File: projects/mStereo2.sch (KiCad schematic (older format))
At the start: 27 parts, among them P101 CONN_AMANERO, P102 MOLEX KK 1x2, P103 MOLEX KK 1X3, P104 NC3MAHL, P105 NC3MAHL, U101 ISO7640, U102 CDCLVC1104, U103 MCP100-315DI, U104 SRC4192, X101 XTAL

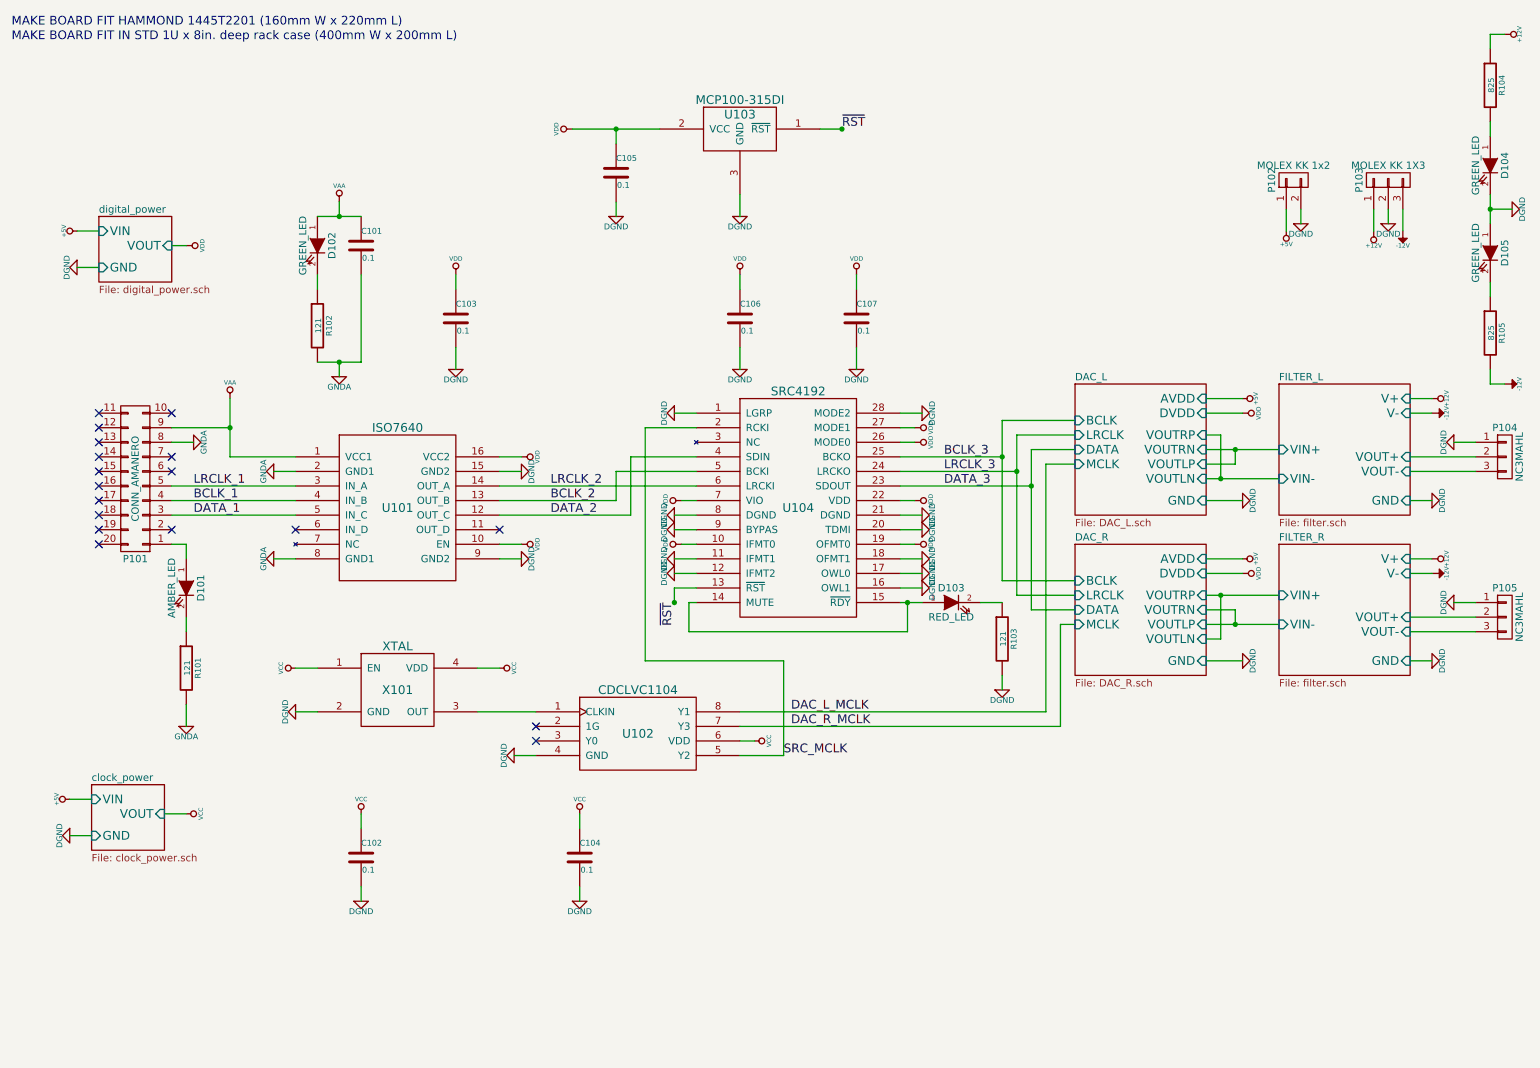
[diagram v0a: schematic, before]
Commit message: update XLR connector part.  Netlist now outdated.
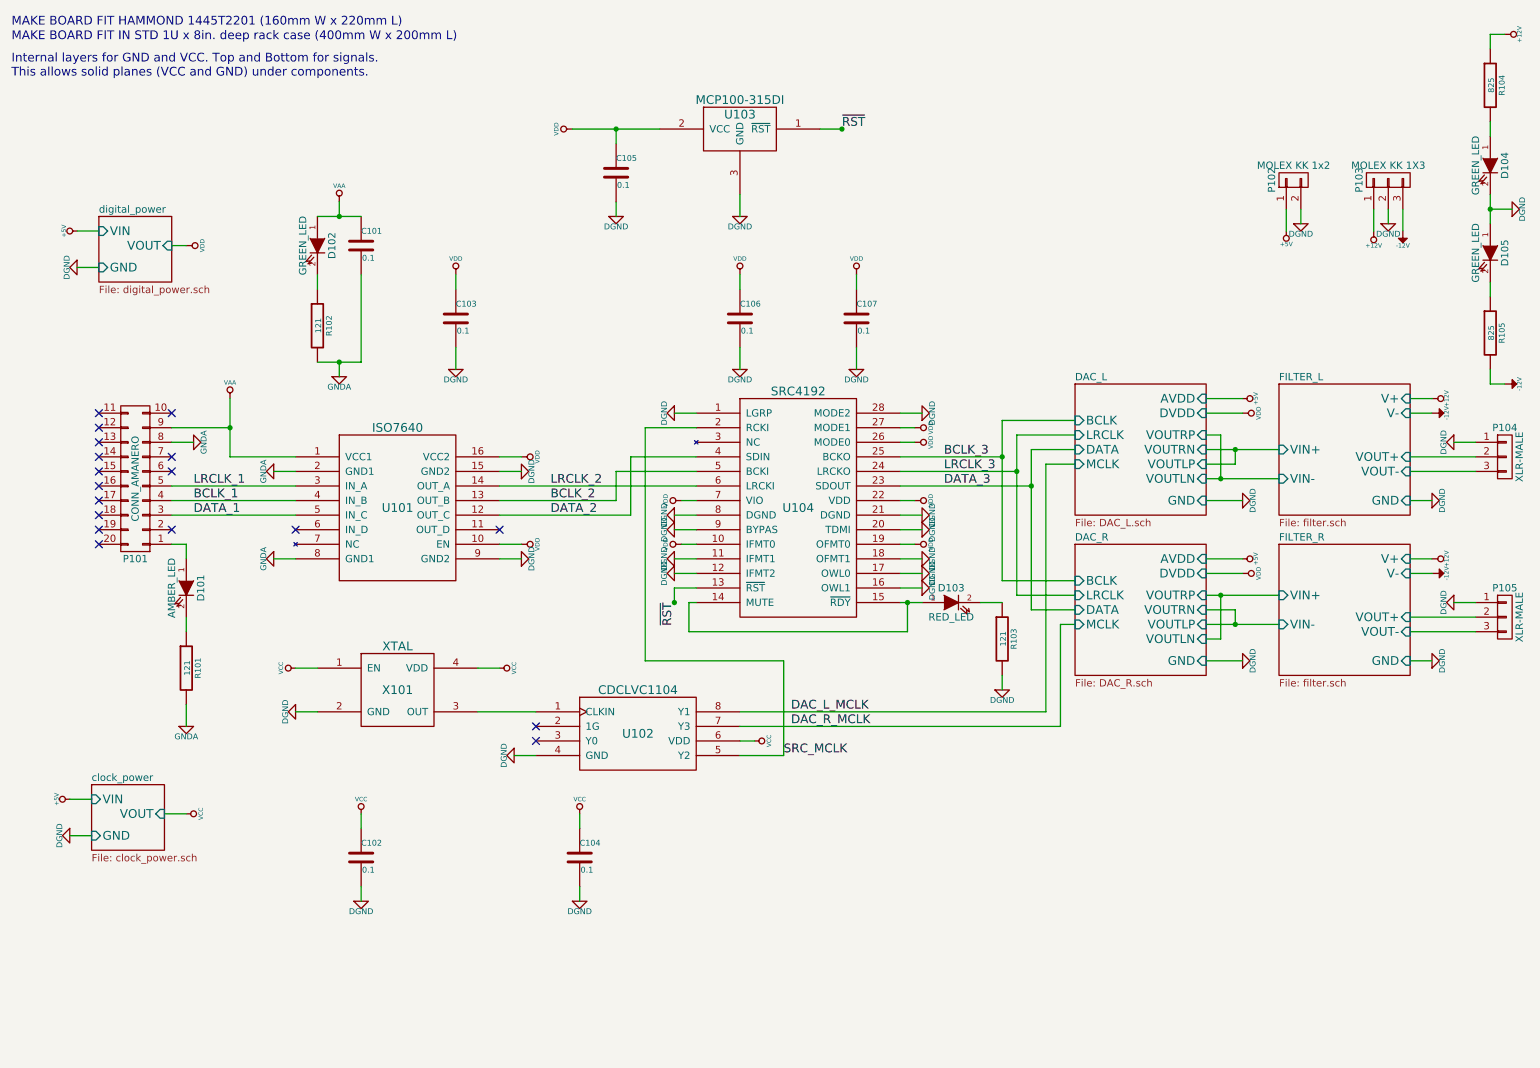
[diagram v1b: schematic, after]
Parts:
- P104, P105: value NC3MAHL -> XLR-MALE; Description XLR connectors 3C MALE COMBO -> XLR Connectors 3P MALE CHASS HORIZONTAL 1; Manu-PN NC3MAHL -> NC3MAAH-1; Supplier-PN 568-NC3MAHL -> 568-NC3MAAH-1
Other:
- note added: "Internal layers for GND and VCC. Top and Bottom for signals.\nThis allows solid planes (VCC and GND) under components."
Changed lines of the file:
@@
 LIBS:oscillator_gosselin
 LIBS:wolfson_gosselin
-LIBS:analog_devices_gosselin
 LIBS:power
 LIBS:device
@@
 LIBS:microchip_gosselin
 LIBS:linear_technology_gosselin
+LIBS:led_gosselin
 LIBS:mStereo2-cache
 EELAYER 24 0
@@
 P 10800 3600
 F 0 "P104" H 10800 3800 50  0000 C CNN
-F 1 "NC3MAHL" V 10900 3600 50  0000 C CNN
+F 1 "XLR-MALE" V 10900 3600 50  0000 C CNN
 F 2 "" H 10800 3600 60  0000 C CNN
 F 3 "" H 10800 3600 60  0000 C CNN
 F 4 "Mouser" H 10800 3600 60  0001 C CNN "Supplier"
-F 5 "568-NC3MAHL" H 10800 3600 60  0001 C CNN "Supplier-PN"
+F 5 "568-NC3MAAH-1" H 10800 3600 60  0001 C CNN "Supplier-PN"
 F 6 "Neutrik" H 10800 3600 60  0001 C CNN "Manu"
-F 7 "NC3MAHL" H 10800 3600 60  0001 C CNN "Manu-PN"
-F 8 "XLR connectors 3C MALE COMBO" H 10800 3600 60  0001 C CNN "Description"
+F 7 "NC3MAAH-1" H 10800 3600 60  0001 C CNN "Manu-PN"
+F 8 "XLR Connectors 3P MALE CHASS HORIZONTAL 1" H 10800 3600 60  0001 C CNN "Description"
 	1    10800 3600
 	1    0    0    -1
@@
 	1    0    0    -1
 $EndComp
-$Comp
-L CONN_01X03 P105
-U 1 1 543297CE
-P 10800 4700
-F 0 "P105" H 10800 4900 50  0000 C CNN
-F 1 "NC3MAHL" V 10900 4700 50  0000 C CNN
-F 2 "" H 10800 4700 60  0000 C CNN
-F 3 "" H 10800 4700 60  0000 C CNN
-F 4 "Mouser" H 10800 4700 60  0001 C CNN "Supplier"
-F 5 "568-NC3MAHL" H 10800 4700 60  0001 C CNN "Supplier-PN"
-F 6 "Neutrik" H 10800 4700 60  0001 C CNN "Manu"
-F 7 "NC3MAHL" H 10800 4700 60  0001 C CNN "Manu-PN"
-F 8 "XLR connectors 3C MALE COMBO" H 10800 4700 60  0001 C CNN "Description"
-	1    10800 4700
-	1    0    0    -1
-$EndComp
 Text Notes 550  650  0    60   ~ 0
 MAKE BOARD FIT HAMMOND 1445T2201 (160mm W x 220mm L)
@@
 	2800 2950 2800 3050
 Wire Wire Line
-	2650 2950 2950 2950
+	2650 2950 2800 2950
+Wire Wire Line
+	2800 2950 2950 2950
 Connection ~ 2800 1950
 Wire Wire Line
 	2800 1850 2800 1950
 Wire Wire Line
-	2650 1950 2950 1950
+	2650 1950 2800 1950
+Wire Wire Line
+	2800 1950 2950 1950
 Wire Wire Line
 	2650 2350 2650 2450
@@
 	10700 3000 10700 3100
 Wire Wire Line
-	10700 1800 10700 2000
+	10700 1800 10700 1900
+Wire Wire Line
+	10700 1900 10700 2000
 Wire Wire Line
 	9900 1900 9900 2050
@@
 	4700 1450 4700 1350
 Wire Wire Line
-	4400 1350 5000 1350
+	4400 1350 4700 1350
+Wire Wire Line
+	4700 1350 5000 1350
 Wire Wire Line
 	10150 5000 10300 5000
@@
 Connection ~ 8950 3550
 Wire Wire Line
-	8750 4550 9250 4550
+	8750 4550 8850 4550
+Wire Wire Line
+	8850 4550 9250 4550
 Wire Wire Line
 	4450 6550 4450 6650
@@
 	2500 3900 1650 3900
 Wire Wire Line
-	2050 3200 2050 3600
+	2050 3200 2050 3400
+Wire Wire Line
+	2050 3400 2050 3600
 Wire Wire Line
 	1650 3800 2500 3800
@@
 	6700 4800 6700 4600
 Wire Wire Line
-	6650 4600 6800 4600
+	6650 4600 6700 4600
+Wire Wire Line
+	6700 4600 6800 4600
 Wire Wire Line
 	5100 3300 5250 3300
@@
 	6650 3600 7350 3600
 Wire Wire Line
-	7350 3350 7350 4450
+	7350 3350 7350 3600
+Wire Wire Line
+	7350 3600 7350 4450
 Wire Wire Line
 	7350 3350 7850 3350
@@
 	6650 3700 7450 3700
 Wire Wire Line
-	7450 3450 7450 4550
+	7450 3450 7450 3700
+Wire Wire Line
+	7450 3700 7450 4550
 Wire Wire Line
 	7450 3450 7850 3450
@@
 	6650 3800 7550 3800
 Wire Wire Line
-	7550 3550 7550 4650
+	7550 3550 7550 3800
+Wire Wire Line
+	7550 3800 7550 4650
 Wire Wire Line
 	7550 3550 7850 3550
@@
 	8850 3450 8850 3750
 Wire Wire Line
-	8750 3750 9250 3750
-Wire Wire Line
-	8750 3550 9250 3550
+	8750 3750 8850 3750
+Wire Wire Line
+	8850 3750 9250 3750
+Wire Wire Line
+	8750 3550 8950 3550
+Wire Wire Line
+	8950 3550 9250 3550
 Wire Wire Line
 	8950 3650 8950 3550
@@
 	8950 4750 8950 4650
 Wire Wire Line
-	8750 4750 9250 4750
+	8750 4750 8950 4750
+Wire Wire Line
+	8950 4750 9250 4750
 $Comp
 L DGND #PWR075
@@
 Text Notes 550  750  0    60   ~ 0
 MAKE BOARD FIT IN STD 1U x 8in. deep rack case (400mm W x 200mm L)
+Text Notes 550  1000 0    60   ~ 0
+Internal layers for GND and VCC. Top and Bottom for signals.\nThis allows solid planes (VCC and GND) under components.
+$Comp
+L CONN_01X03 P105
+U 1 1 54769445
+P 10800 4700
+F 0 "P105" H 10800 4900 50  0000 C CNN
+F 1 "XLR-MALE" V 10900 4700 50  0000 C CNN
+F 2 "" H 10800 4700 60  0000 C CNN
+F 3 "" H 10800 4700 60  0000 C CNN
+F 4 "Mouser" H 10800 4700 60  0001 C CNN "Supplier"
+F 5 "568-NC3MAAH-1" H 10800 4700 60  0001 C CNN "Supplier-PN"
+F 6 "Neutrik" H 10800 4700 60  0001 C CNN "Manu"
+F 7 "NC3MAAH-1" H 10800 4700 60  0001 C CNN "Manu-PN"
+F 8 "XLR Connectors 3P MALE CHASS HORIZONTAL 1" H 10800 4700 60  0001 C CNN "Description"
+	1    10800 4700
+	1    0    0    -1
+$EndComp
 $EndSCHEMATC

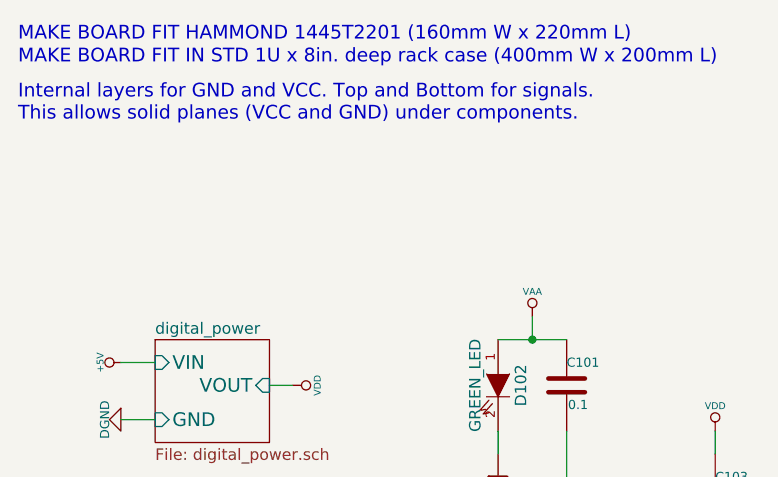
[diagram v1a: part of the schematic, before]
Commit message: update schematic notes
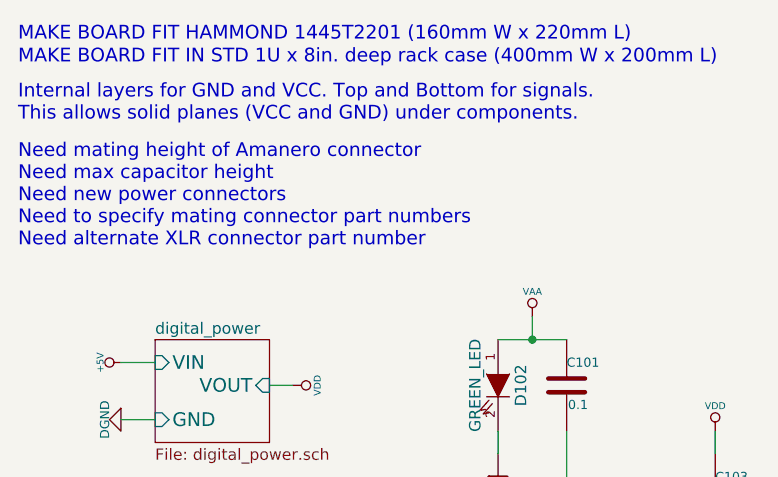
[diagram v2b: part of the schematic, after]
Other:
- note added: "Need mating height of Amanero connector\nNeed max capacitor height\nNeed new power connectors\nNeed to specify mating connector part numbers\nNeed alternate XLR connector part number\n"
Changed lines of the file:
@@
 	1    0    0    -1
 $EndComp
+Text Notes 550  1550 0    60   ~ 0
+Need mating height of Amanero connector\nNeed max capacitor height\nNeed new power connectors\nNeed to specify mating connector part numbers\nNeed alternate XLR connector part number\n
 $EndSCHEMATC

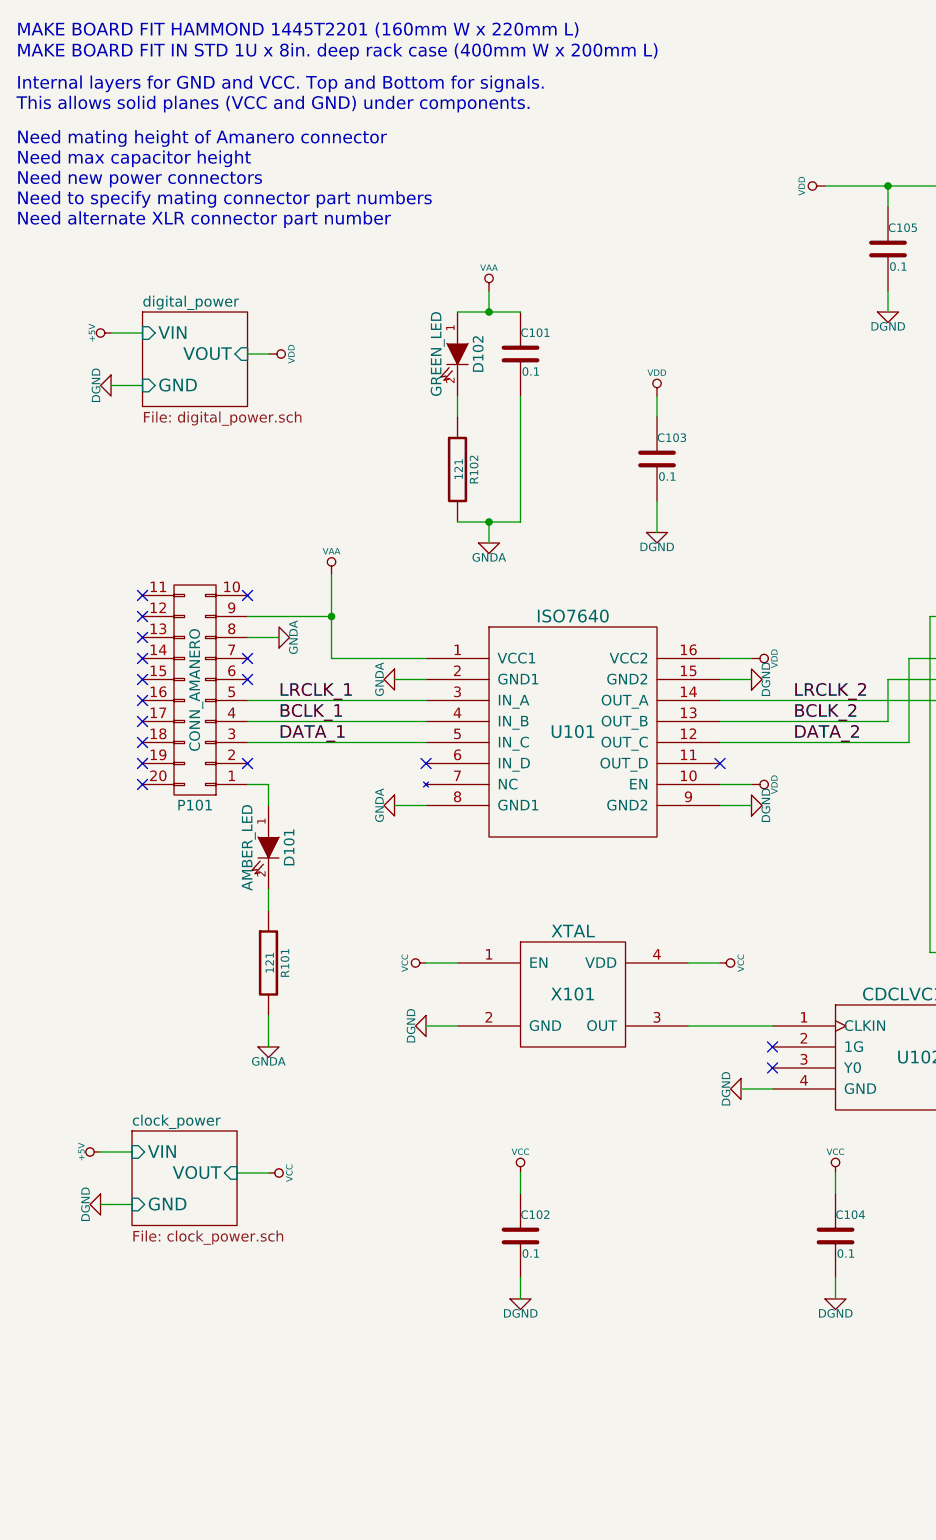
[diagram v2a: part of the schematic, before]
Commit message: updated notes with mating connector part numbers
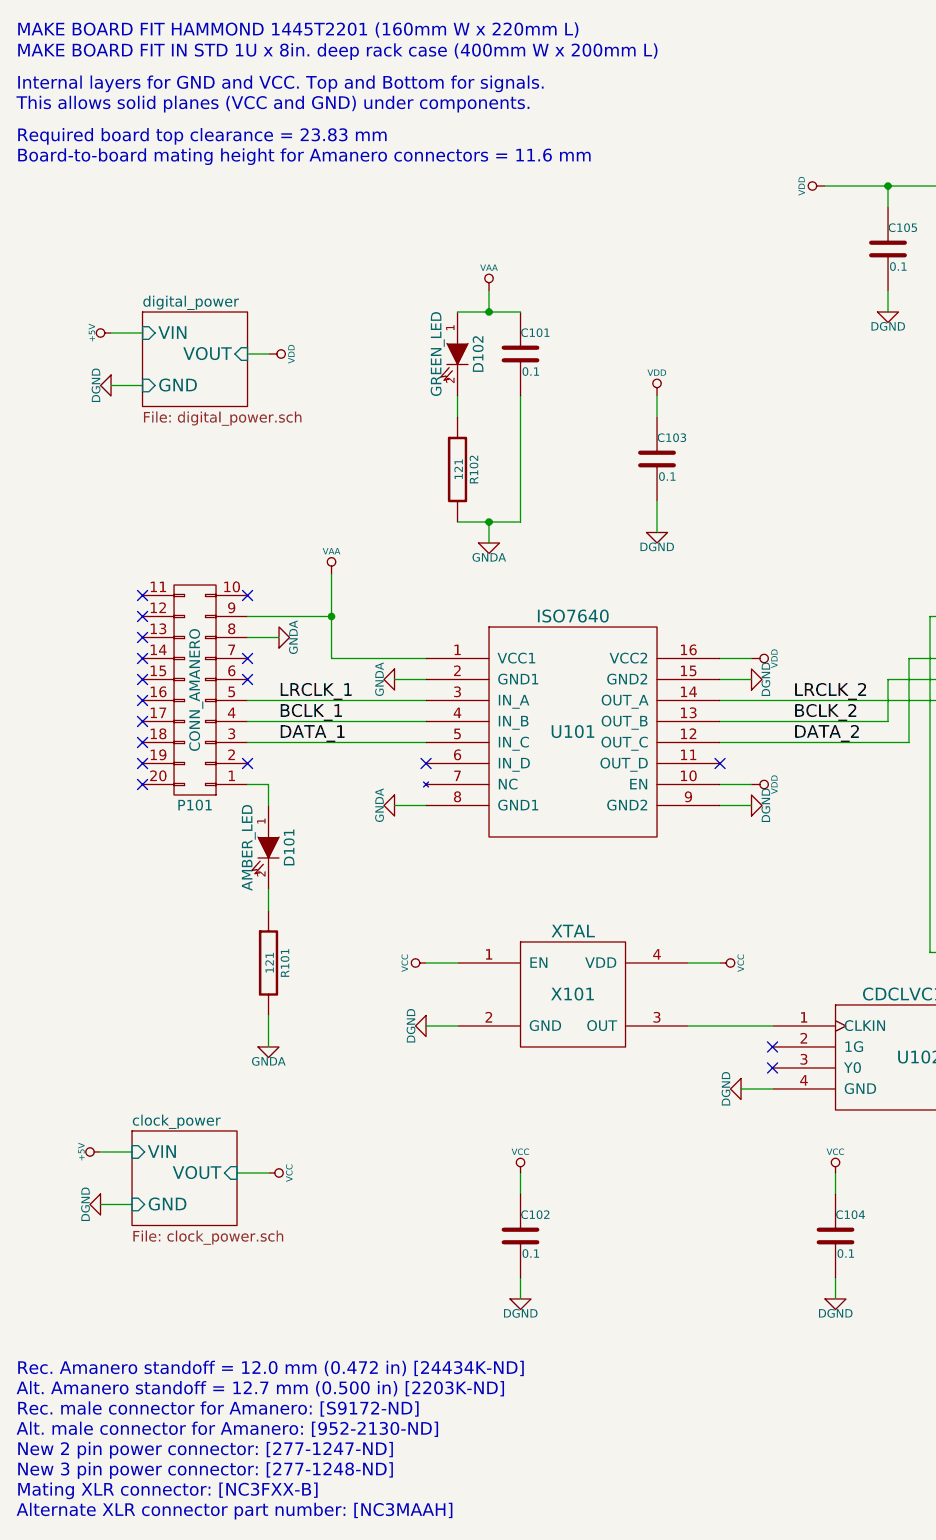
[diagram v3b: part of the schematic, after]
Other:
- note added: "Rec. Amanero standoff = 12.0 mm (0.472 in) [24434K-ND]\nAlt. Amanero standoff = 12.7 mm (0.500 in) [2203K-ND]\nRec. male connector for Amanero: [S9172-ND]\nAlt. male connector for Amanero: [952-2130-ND]\nNew 2 pin power connector: [277-1247-ND]\nNew 3 pin power connector: [277-1248-ND]\nMating XLR connector: [NC3FXX-B]\nAlternate XLR connector part number: [NC3MAAH]\n"
- note added: "Required board top clearance = 23.83 mm\nBoard-to-board mating height for Amanero connectors = 11.6 mm\n"
- note removed: "Need mating height of Amanero connector\nNeed max capacitor height\nNeed new power connectors\nNeed to specify mating connector part numbers\nNeed alternate XLR connector part number\n"
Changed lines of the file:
@@
 	1    0    0    -1
 $EndComp
-Text Notes 550  1550 0    60   ~ 0
-Need mating height of Amanero connector\nNeed max capacitor height\nNeed new power connectors\nNeed to specify mating connector part numbers\nNeed alternate XLR connector part number\n
+Text Notes 550  7700 0    60   ~ 0
+Rec. Amanero standoff = 12.0 mm (0.472 in) [24434K-ND]\nAlt. Amanero standoff = 12.7 mm (0.500 in) [2203K-ND]\nRec. male connector for Amanero: [S9172-ND]\nAlt. male connector for Amanero: [952-2130-ND]\nNew 2 pin power connector: [277-1247-ND]\nNew 3 pin power connector: [277-1248-ND]\nMating XLR connector: [NC3FXX-B]\nAlternate XLR connector part number: [NC3MAAH]\n
+Text Notes 550  1250 0    60   ~ 0
+Required board top clearance = 23.83 mm\nBoard-to-board mating height for Amanero connectors = 11.6 mm\n
 $EndSCHEMATC
